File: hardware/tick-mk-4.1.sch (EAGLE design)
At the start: 15 parts, among them U1 ATMEGA328P

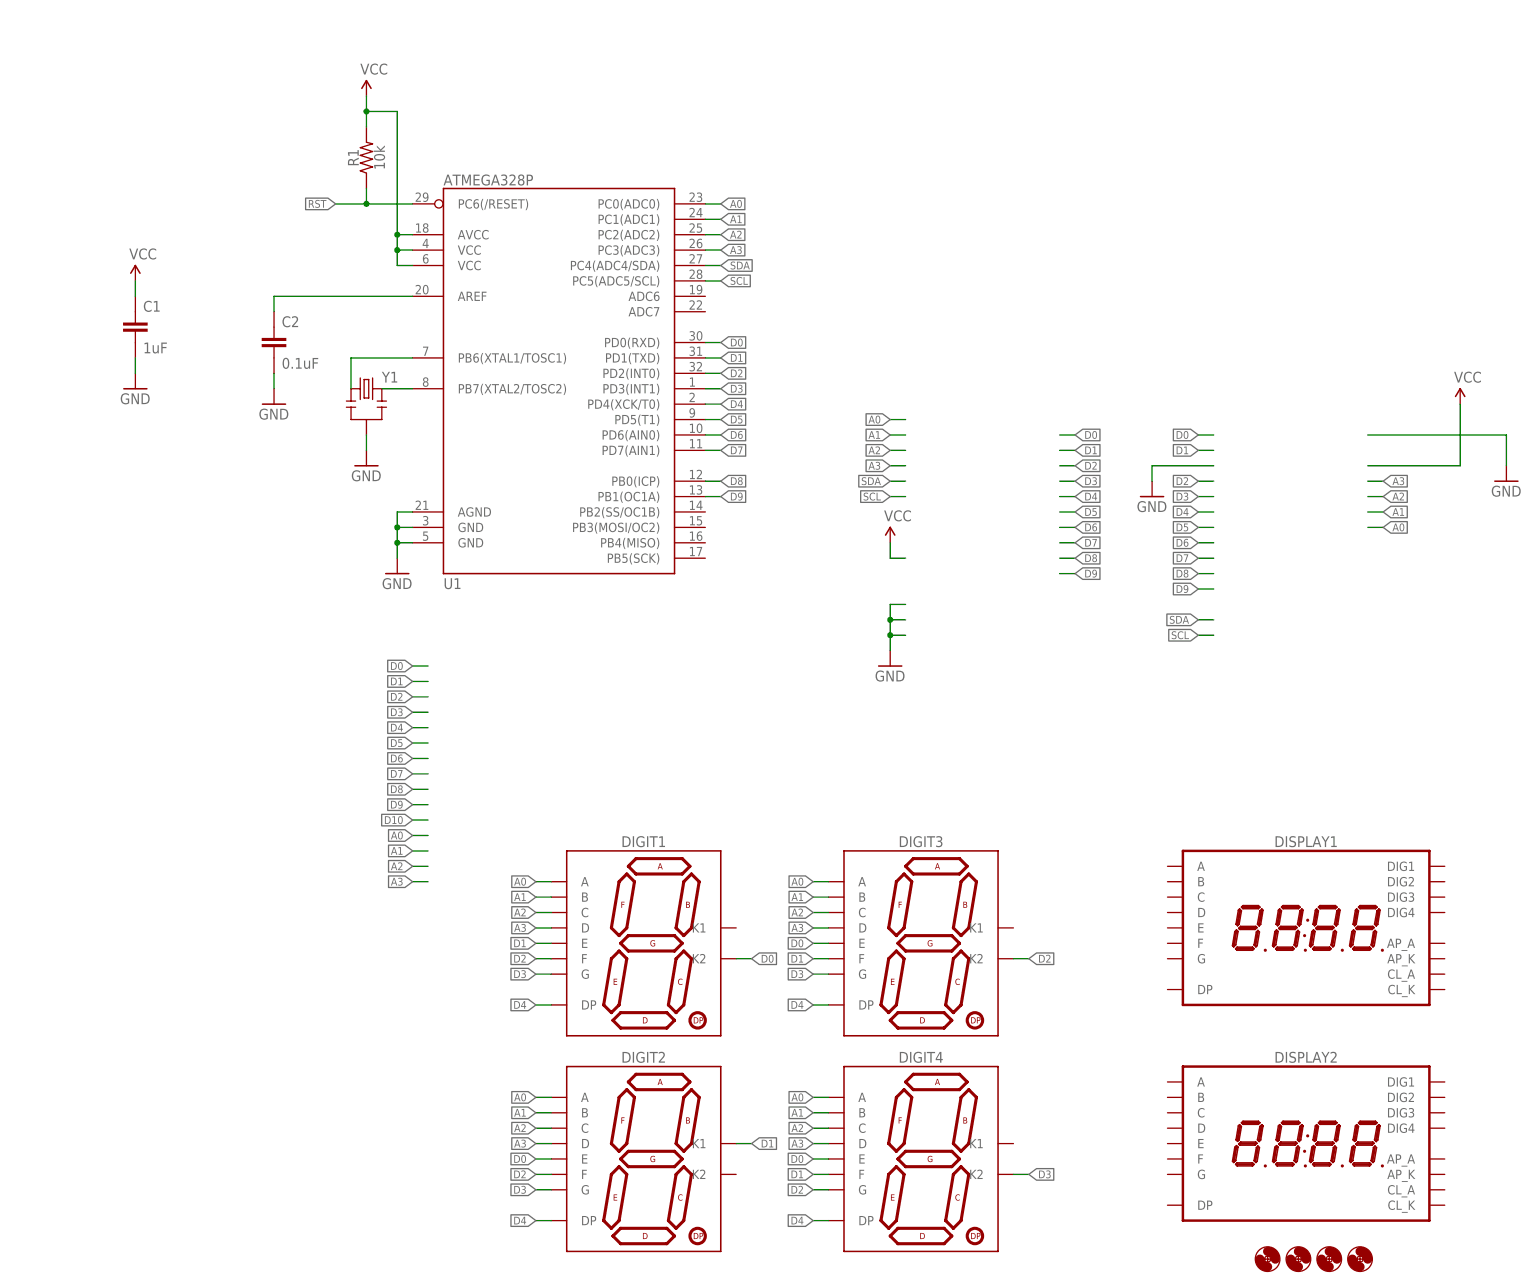
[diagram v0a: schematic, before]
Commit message: routed and RTC chip added
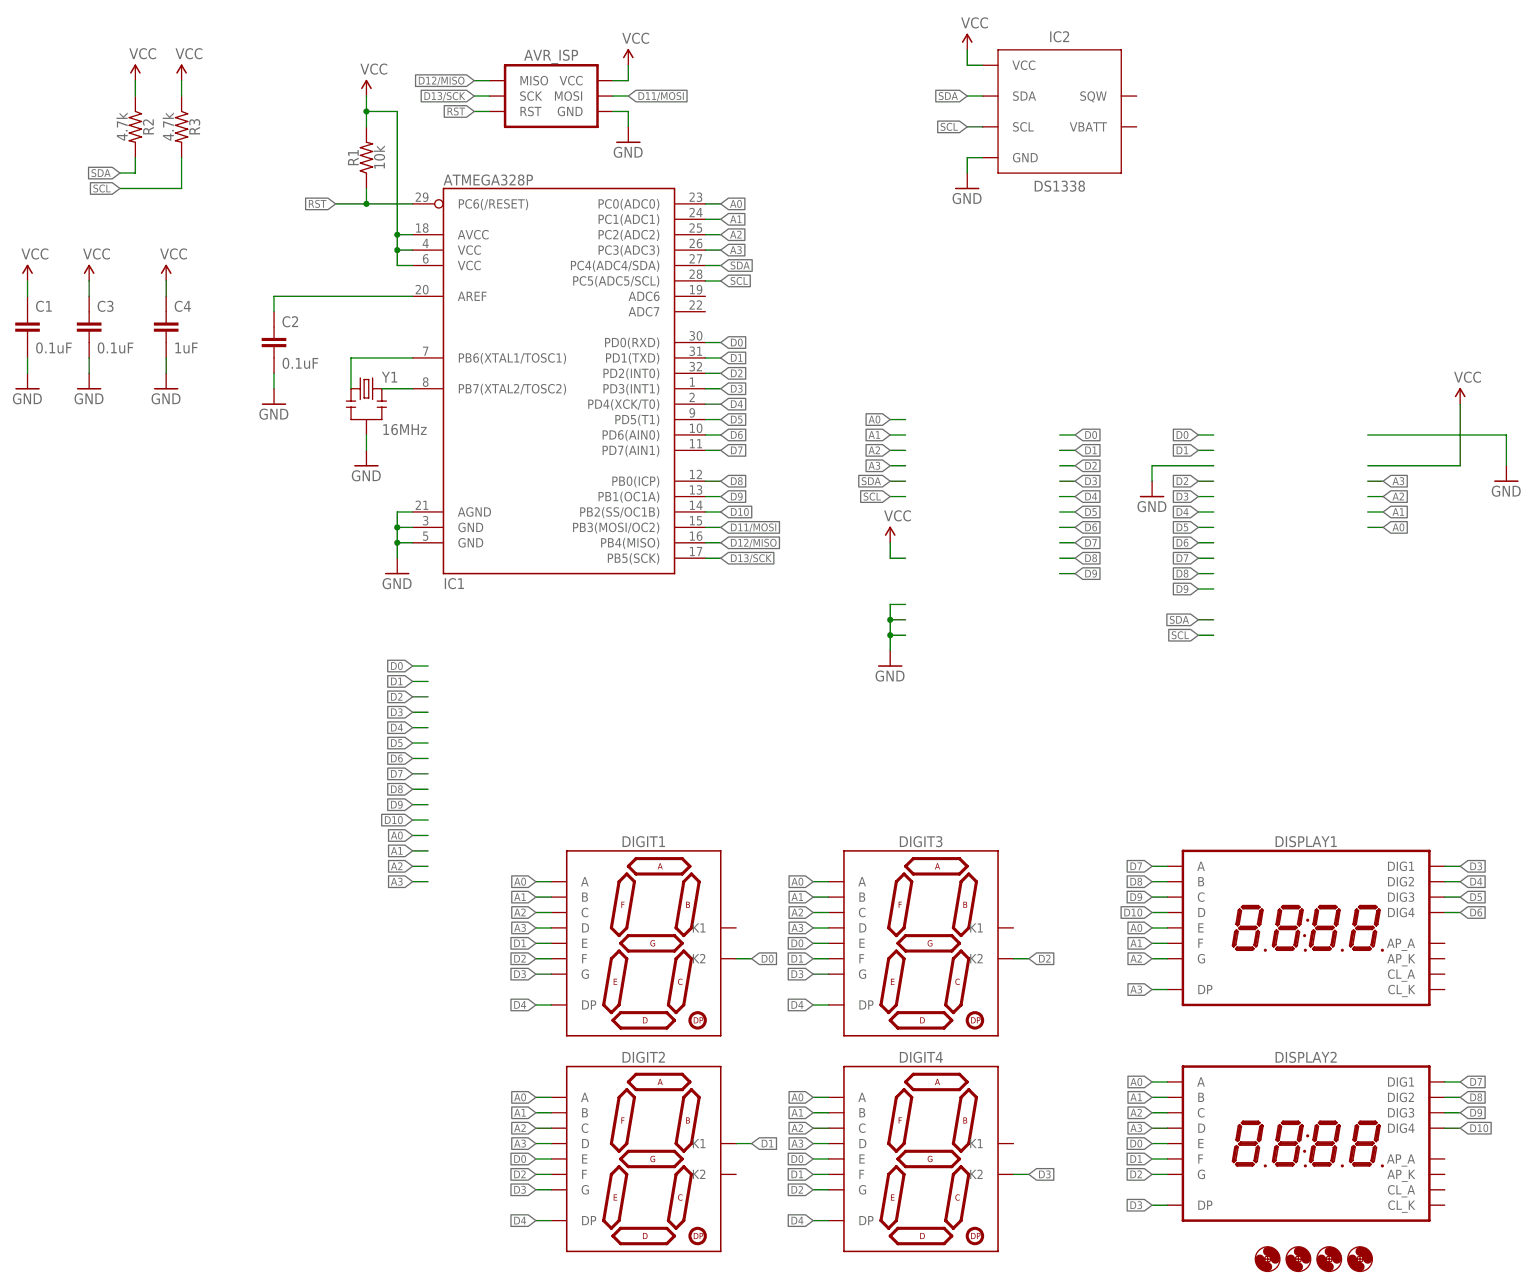
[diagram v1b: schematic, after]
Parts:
- added AVR_ISP: AVR_SPI_PRG_6PTH, A_butts:AVR_SPI_PRG_6PTH
- added C3: 0.1uF, A_butts:CAPACITOR-CERAMICC0805
- added C4: 1uF, A_butts:CAPACITOR-CERAMICC0805
- added IC2: DS1338, A_butts:DS1338CSOIC16W
- added R2, R3: 4.7k, A_butts:RESISTORR0805
- C1: value 1uF -> 0.1uF
- Y1: value (none) -> 16MHz
- renumbered U1 to IC1
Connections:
- new net D10: DISPLAY1.D, DISPLAY2.DIG4, IC1.PB2(SS/OC1B)
- new net D11/MOSI: AVR_ISP.MOSI, IC1.PB3(MOSI/OC2)
- new net D12/MISO: AVR_ISP.MISO, IC1.PB4(MISO)
- new net D13/SCK: AVR_ISP.SCK, IC1.PB5(SCK)
- net A0: now also DISPLAY1.E, DISPLAY2.A
- net A1: now also DISPLAY1.F, DISPLAY2.B
- net A2: now also DISPLAY1.G, DISPLAY2.C
- net A3: now also DISPLAY1.DP, DISPLAY2.D
- net D0: now also DISPLAY2.E
- net D1: now also DISPLAY2.F
- net D2: now also DISPLAY2.G
- net D3: now also DISPLAY1.DIG1, DISPLAY2.DP
- net D4: now also DISPLAY1.DIG2
- net D5: now also DISPLAY1.DIG3
- net D6: now also DISPLAY1.DIG4
- net D7: now also DISPLAY1.A, DISPLAY2.DIG1
- net D8: now also DISPLAY1.B, DISPLAY2.DIG2
- net D9: now also DISPLAY1.C, DISPLAY2.DIG3
- net GND: now also AVR_ISP.GND, C3.2, C4.2, IC2.GND
- net RST: now also AVR_ISP.RST
- net SCL: now also IC2.SCL, R3.2
- net SDA: now also IC2.SDA, R2.2
- net VCC: now also AVR_ISP.VCC, C3.1, C4.1, IC2.VCC, R2.1, R3.1
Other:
- moved on the sheet: C1
